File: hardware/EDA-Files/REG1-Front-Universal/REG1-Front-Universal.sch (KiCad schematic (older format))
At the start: 9 parts, among them J1 Conn_02x04_Odd_Even, SW1 Prog, SW2 Func, SW3 Res, SW4 BL

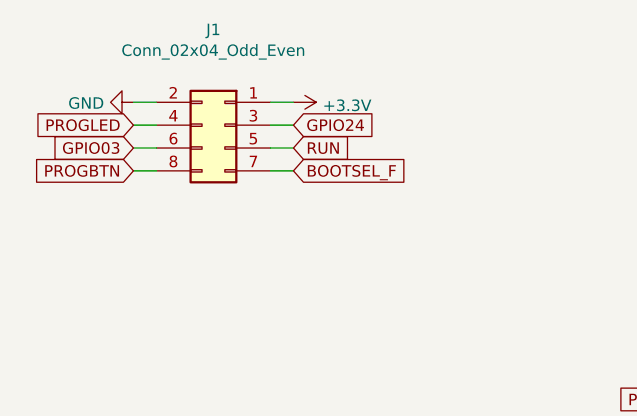
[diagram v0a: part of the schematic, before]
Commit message: rotate connector, rotate switches, 0.2mm smaller on each side, corrected pinout of connector
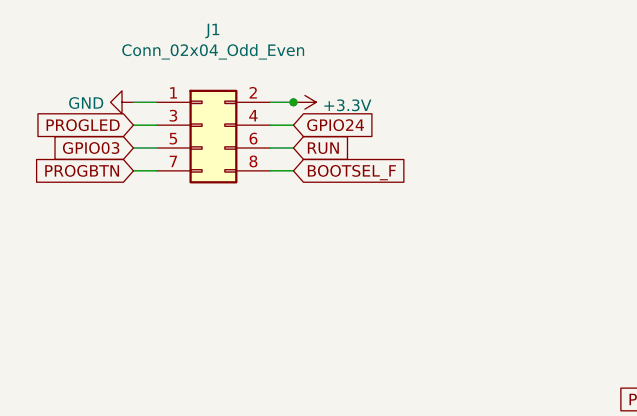
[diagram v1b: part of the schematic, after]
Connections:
- net +3V3: now also J1.2 (Pin_2); no longer J1.1 (Pin_1)
- net BOOTSEL_F: now also J1.8 (Pin_8); no longer J1.7 (Pin_7)
- net GND: now also J1.1 (Pin_1); no longer J1.2 (Pin_2)
- net GPIO03: now also J1.5 (Pin_5); no longer J1.6 (Pin_6)
- net GPIO24: now also J1.4 (Pin_4); no longer J1.3 (Pin_3)
- net PROGBTN: now also J1.7 (Pin_7); no longer J1.8 (Pin_8)
- net PROGLED: now also J1.3 (Pin_3); no longer J1.4 (Pin_4)
- net RUN: now also J1.6 (Pin_6); no longer J1.5 (Pin_5)
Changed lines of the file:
@@
 EESchema Schematic File Version 4
+LIBS:REG1-Front-Universal-cache
 EELAYER 30 0
 EELAYER END
@@
 Sheet 1 1
 Title "REG1-Front-Universal"
-Date "2022-10-21"
-Rev "V00.01"
+Date "2022-11-04"
+Rev "V00.02"
 Comp "OpenKNX"
 Comment1 "by SirSydom <com@sirsydom.de>"
@@
 L Connector_Generic:Conn_02x04_Odd_Even J?
 U 1 1 63548ED5
-P 2350 1650
+P 2250 1650
 AR Path="/5FE0DFF8/63548ED5" Ref="J?"  Part="1"
 AR Path="/63548ED5" Ref="J1"  Part="1"
-F 0 "J1" H 2400 2067 50  0000 C CNN
-F 1 "Conn_02x04_Odd_Even" H 2400 1976 50  0000 C CNN
-F 2 "Connector_PinHeader_2.00mm:PinHeader_2x04_P2.00mm_Vertical_SMD" H 2350 1650 50  0001 C CNN
-F 3 "~" H 2350 1650 50  0001 C CNN
-	1    2350 1650
-	-1   0    0    -1
+F 0 "J1" H 2300 2067 50  0000 C CNN
+F 1 "Conn_02x04_Odd_Even" H 2300 1976 50  0000 C CNN
+F 2 "Connector_PinHeader_2.00mm:PinHeader_2x04_P2.00mm_Vertical_SMD" H 2250 1650 50  0001 C CNN
+F 3 "~" H 2250 1650 50  0001 C CNN
+	1    2250 1650
+	1    0    0    -1
 $EndComp
 Text GLabel 2650 1650 2    50   Input ~ 0
@@
 Wire Wire Line
 	4500 3300 4700 3300
+Connection ~ 2650 1550
 $EndSCHEMATC

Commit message: Front V00.02
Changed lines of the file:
@@
 Rev "V00.02"
 Comp "OpenKNX"
-Comment1 "by SirSydom <com@sirsydom.de>"
+Comment1 "by Ing-Dom <dom@ing-dom.de>"
 Comment2 ""
 Comment3 ""
@@
 Wire Wire Line
 	4500 3300 4700 3300
-Connection ~ 2650 1550
 $EndSCHEMATC

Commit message: REG1-Front-Universal V01.00
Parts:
- added J2: Conn_01x10, sirsydom:C11050_FPC-SMD_P0.5-10P_LSXJ-H2.0-10P, symbol Connector_Generic:Conn_01x10
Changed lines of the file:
@@
 EESchema Schematic File Version 4
-LIBS:REG1-Front-Universal-cache
 EELAYER 30 0
 EELAYER END
@@
 Wire Wire Line
 	4500 3300 4700 3300
+$Comp
+L Connector_Generic:Conn_01x10 J2
+U 1 1 64A2C9EB
+P 2100 3050
+F 0 "J2" H 2180 3042 50  0000 L CNN
+F 1 "Conn_01x10" H 2180 2951 50  0000 L CNN
+F 2 "sirsydom:C11050_FPC-SMD_P0.5-10P_LSXJ-H2.0-10P" H 2100 3050 50  0001 C CNN
+F 3 "~" H 2100 3050 50  0001 C CNN
+	1    2100 3050
+	1    0    0    -1
+$EndComp
 $EndSCHEMATC
